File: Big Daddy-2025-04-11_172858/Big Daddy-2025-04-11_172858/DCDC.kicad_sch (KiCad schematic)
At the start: 16 parts, among them U10 TLP184, U8 Vicor_AERO, U9 LTV-817S

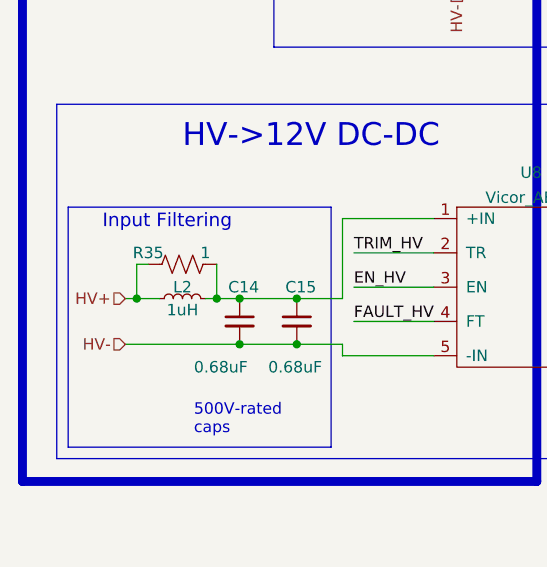
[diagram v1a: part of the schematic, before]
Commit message: PCB fixes
BMS relay
C12 footprint
TSMP resistor connections
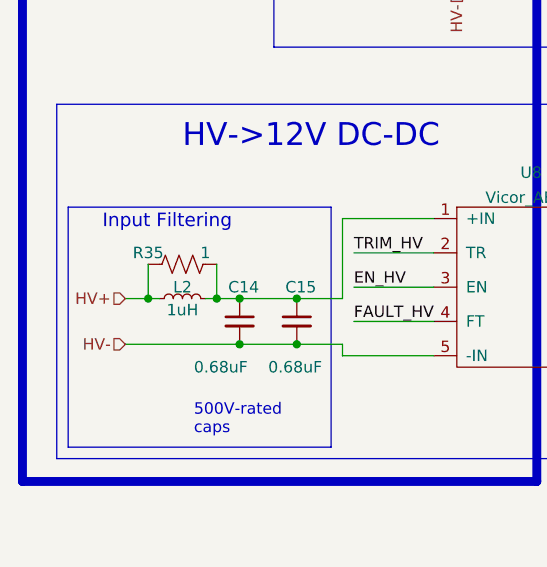
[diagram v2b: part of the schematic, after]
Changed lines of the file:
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@@
+	)
+	(junction
+		(at 79.756 135.89)
+		(diameter 0)
+		(color 0 0 0 0)
 	)
 	(junction
@@
 	)
 	(junction
-		(at 78.486 135.89)
-		(diameter 0)
-		(color 0 0 0 0)
-	)
-	(junction
 		(at 145.796 132.08)
 		(diameter 0)
@@
 	(wire
 		(pts
-			(xy 78.486 132.08) (xy 78.486 135.89)
-		)
-		(stroke
-			(width 0)
-			(type default)
-		)
-	)
-	(wire
-		(pts
 			(xy 115.316 99.06) (xy 114.046 99.06)
 		)
@@
 	(wire
 		(pts
+			(xy 79.756 135.89) (xy 81.026 135.89)
+		)
+		(stroke
+			(width 0)
+			(type default)
+		)
+	)
+	(wire
+		(pts
 			(xy 130.556 93.98) (xy 139.446 93.98)
 		)
@@
 	(wire
 		(pts
-			(xy 79.756 132.08) (xy 78.486 132.08)
-		)
-		(stroke
-			(width 0)
-			(type default)
-		)
-	)
-	(wire
-		(pts
 			(xy 157.226 124.46) (xy 157.226 132.08)
 		)
@@
 	(wire
 		(pts
-			(xy 78.486 135.89) (xy 77.216 135.89)
-		)
-		(stroke
-			(width 0)
-			(type default)
-		)
-	)
-	(wire
-		(pts
 			(xy 149.606 132.08) (xy 149.606 124.46)
 		)
@@
 		)
 	)
+	(wire
+		(pts
+			(xy 79.756 132.08) (xy 79.756 135.89)
+		)
+		(stroke
+			(width 0)
+			(type default)
+		)
+	)
 	(polyline
 		(pts
@@
 	(wire
 		(pts
-			(xy 78.486 135.89) (xy 81.026 135.89)
-		)
-		(stroke
-			(width 0)
-			(type default)
-		)
-	)
-	(wire
-		(pts
 			(xy 89.916 140.97) (xy 96.266 140.97)
 		)
@@
 		)
 		(stroke
+			(width 0)
+			(type default)
+		)
+	)
+	(wire
+		(pts
+			(xy 77.216 135.89) (xy 79.756 135.89)
+		)
+		(stroke

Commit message: all the bs
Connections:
- no-connect marks 0 -> 1
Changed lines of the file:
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@@
 		(color 0 0 0 0)
 	)
+	(no_connect
+		(at 99.06 38.1)
+	)
 	(polyline
 		(pts
@@
 	(wire
 		(pts
-			(xy 103.886 45.72) (xy 98.806 45.72)
+			(xy 104.14 45.72) (xy 99.06 45.72)
 		)
 		(stroke
@@
 	(wire
 		(pts
-			(xy 79.121 41.91) (xy 87.376 41.91)
+			(xy 79.121 41.91) (xy 87.63 41.91)
 		)
 		(stroke
@@
 	(hierarchical_label "HV-"
 		(shape input)
-		(at 103.886 45.72 0)
+		(at 104.14 45.72 0)
 		(effects
 			(font
@@
 	(symbol
 		(lib_id "Device:R")
-		(at 91.186 41.91 90)
+		(at 91.44 41.91 90)
 		(unit 1)
 		(exclude_from_sim no)
@@
 		(fields_autoplaced yes)
 		(property "Reference" "R36"
-			(at 91.186 36.9275 90)
+			(at 91.44 36.9275 90)
 			(effects
 				(font
@@
 		)
 		(property "Value" "300"
-			(at 91.186 39.7026 90)
+			(at 91.44 39.7026 90)
 			(effects
 				(font
@@
 		)
 		(property "Footprint" "Resistor_SMD:R_0603_1608Metric_Pad0.98x0.95mm_HandSolder"
-			(at 91.186 43.688 90)
+			(at 91.44 43.688 90)
 			(effects
 				(font
@@
 		)
 		(property "Datasheet" "https://industrial.panasonic.com/ww/products/pt/general-purpose-chip-resistors/models/ERJ3GEYJ301V"
-			(at 91.186 41.91 0)
+			(at 91.44 41.91 0)
 			(effects
 				(font
@@
 		)
 		(property "Description" ""
-			(at 91.186 41.91 0)
+			(at 91.44 41.91 0)
 			(effects
 				(font
@@
 		)
 		(property "Digikey part number" "P300GCT-ND"
-			(at 91.186 41.91 0)
+			(at 91.44 41.91 0)
 			(effects
 				(font
@@
 		)
 		(property "Manufacturer_Part_Number" "ERJ-3GEYJ301V"
-			(at 91.186 41.91 0)
+			(at 91.44 41.91 0)
 			(effects
 				(font
@@
 	(symbol
 		(lib_id "Device:R_POT_TRIM_US")
-		(at 98.806 41.91 180)
+		(at 99.06 41.91 180)
 		(unit 1)
 		(exclude_from_sim no)
@@
 		(dnp no)
 		(property "Reference" "RV1"
-			(at 100.5332 43.0784 0)
+			(at 100.7872 43.0784 0)
 			(effects
 				(font
@@
 		)
 		(property "Value" "50k TC33x-2-503E"
-			(at 100.5332 40.767 0)
+			(at 100.7872 40.767 0)
 			(effects
 				(font
@@
 		)
 		(property "Footprint" "Potentiometer_SMD:Potentiometer_Bourns_TC33X_Vertical"
-			(at 98.806 41.91 0)
+			(at 99.06 41.91 0)
 			(effects
 				(font
@@
 		)
 		(property "Datasheet" "https://www.bourns.com/docs/Product-Datasheets/TC33.pdf"
-			(at 98.806 41.91 0)
+			(at 99.06 41.91 0)
 			(effects
 				(font
@@
 		)
 		(property "Description" ""
-			(at 98.806 41.91 0)
+			(at 99.06 41.91 0)
 			(effects
 				(font
@@
 		)
 		(property "Digikey part number" "TC33X-503ECT-ND"
-			(at 98.806 41.91 0)
+			(at 99.06 41.91 0)
 			(effects
 				(font
@@
 		)
 		(property "Manufacturer_Part_Number" "TC33X-2-503E"
-			(at 98.806 41.91 0)
-			(effects
-				(font
+			(at 99.06 41.91 0)
+			(effects
+				(font
